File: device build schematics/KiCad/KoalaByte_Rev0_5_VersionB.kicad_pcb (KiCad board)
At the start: 2 copper layers, 120 x 85 mm, 0 parts

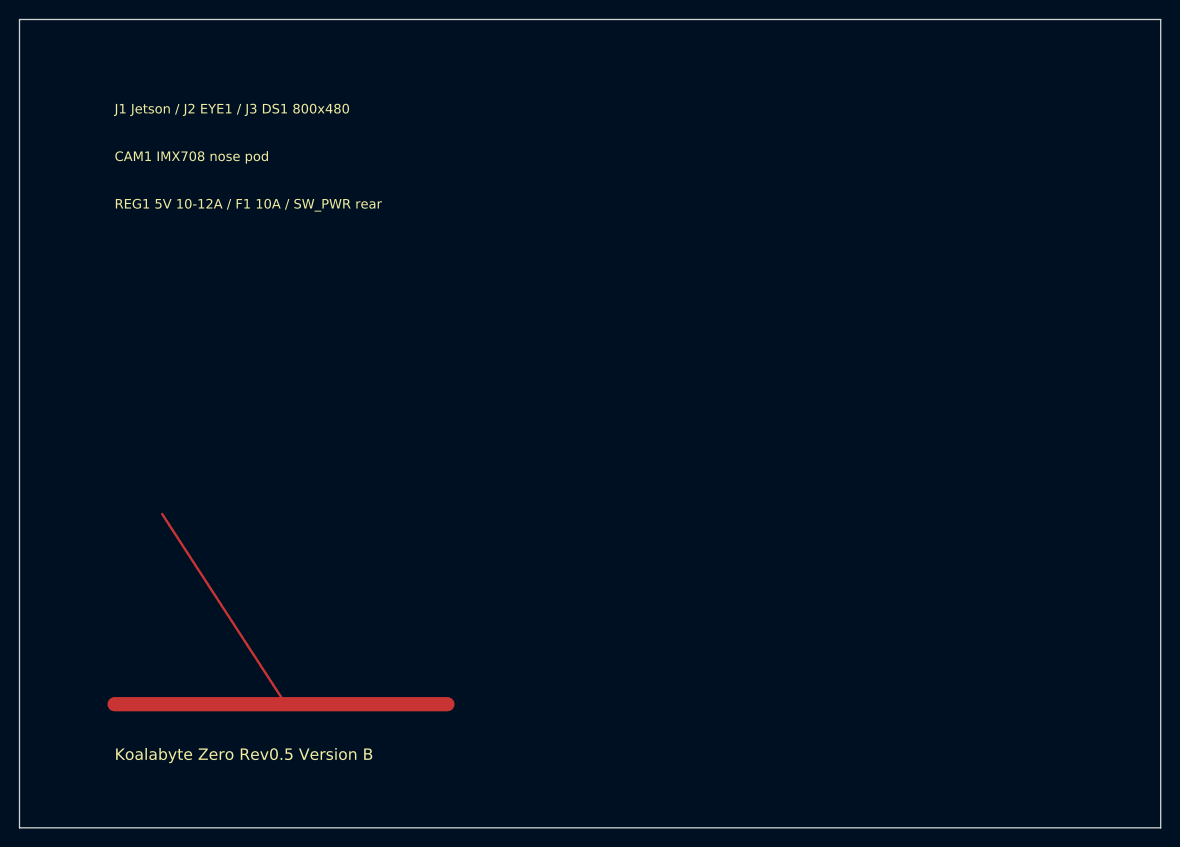
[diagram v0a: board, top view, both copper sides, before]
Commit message: Add MIC1 PCB starter annotation
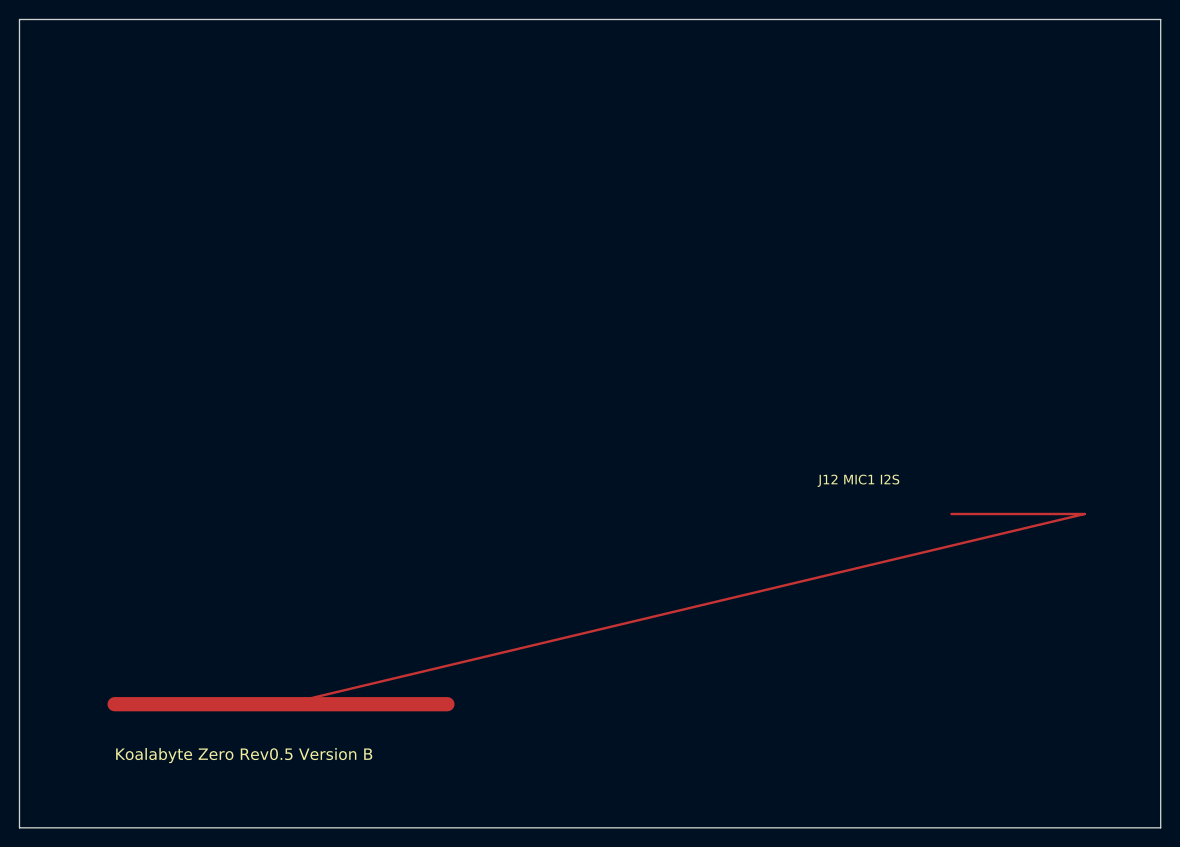
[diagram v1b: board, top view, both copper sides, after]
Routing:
- net +3V3: track 23.9 -> 86.3 mm
- net MIC1_I2S: track 0.00 -> 14.0 mm
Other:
- board text added: "J12 MIC1 I2S"
- board text removed: "CAM1 IMX708 nose pod"
- board text removed: "J1 Jetson / J2 EYE1 / J3 DS1 800x480"
- board text removed: "REG1 5V 10-12A / F1 10A / SW_PWR rear"
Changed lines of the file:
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@@
     (rev "0.5B-normalized")
     (company "Urban Poacher / Koalabyte")
-    (comment 1 "Prototype starter only. Run ERC/DRC, footprint validation, and power review before fabrication.")
-    (comment 2 "DS1 800x480; CAM1 IMX708; REG1 5V 10-12A; F1 10A-class; HUB1; SPK1; rear SW_PWR.")
+    (comment 1 "Prototype starter only")
+    (comment 2 "DS1 CAM1 MIC1 REG1 F1")
   )
   (layers
@@
   (net 2 "+3V3")
   (net 3 "GND")
-  (net 4 "I2C")
-  (net 5 "UART")
-  (net 6 "SPI")
-  (net 7 "IR")
-  (net 8 "BUTTONS")
+  (net 16 "MIC1_I2S")
   (gr_rect (start 0 0) (end 120 85) (stroke (width 0.1) (type default)) (fill none) (layer "Edge.Cuts"))
   (gr_text "Koalabyte Zero Rev0.5 Version B" (at 10 78 0) (layer "F.SilkS") (effects (font (size 1.2 1.2) (thickness 0.15)) (justify left bottom)))
-  (gr_text "J1 Jetson / J2 EYE1 / J3 DS1 800x480" (at 10 10 0) (layer "F.SilkS") (effects (font (size 1 1) (thickness 0.12)) (justify left bottom)))
-  (gr_text "CAM1 IMX708 nose pod" (at 10 15 0) (layer "F.SilkS") (effects (font (size 1 1) (thickness 0.12)) (justify left bottom)))
-  (gr_text "REG1 5V 10-12A / F1 10A / SW_PWR rear" (at 10 20 0) (layer "F.SilkS") (effects (font (size 1 1) (thickness 0.12)) (justify left bottom)))
+  (gr_text "J12 MIC1 I2S" (at 84 49 0) (layer "F.SilkS") (effects (font (size 1 1) (thickness 0.12)) (justify left bottom)))
   (segment (start 10 72) (end 45 72) (width 1.5) (layer "F.Cu") (net 1))
-  (segment (start 28 72) (end 15 52) (width 0.25) (layer "F.Cu") (net 2))
+  (segment (start 28 72) (end 112 52) (width 0.25) (layer "F.Cu") (net 2))
+  (segment (start 112 52) (end 98 52) (width 0.25) (layer "F.Cu") (net 16))
 )
